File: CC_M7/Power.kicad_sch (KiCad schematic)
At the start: 18 parts, among them J13 Batt_Pins, U10 ME6211C33M5, U8 TPS562206, U9 ME6211C33M5

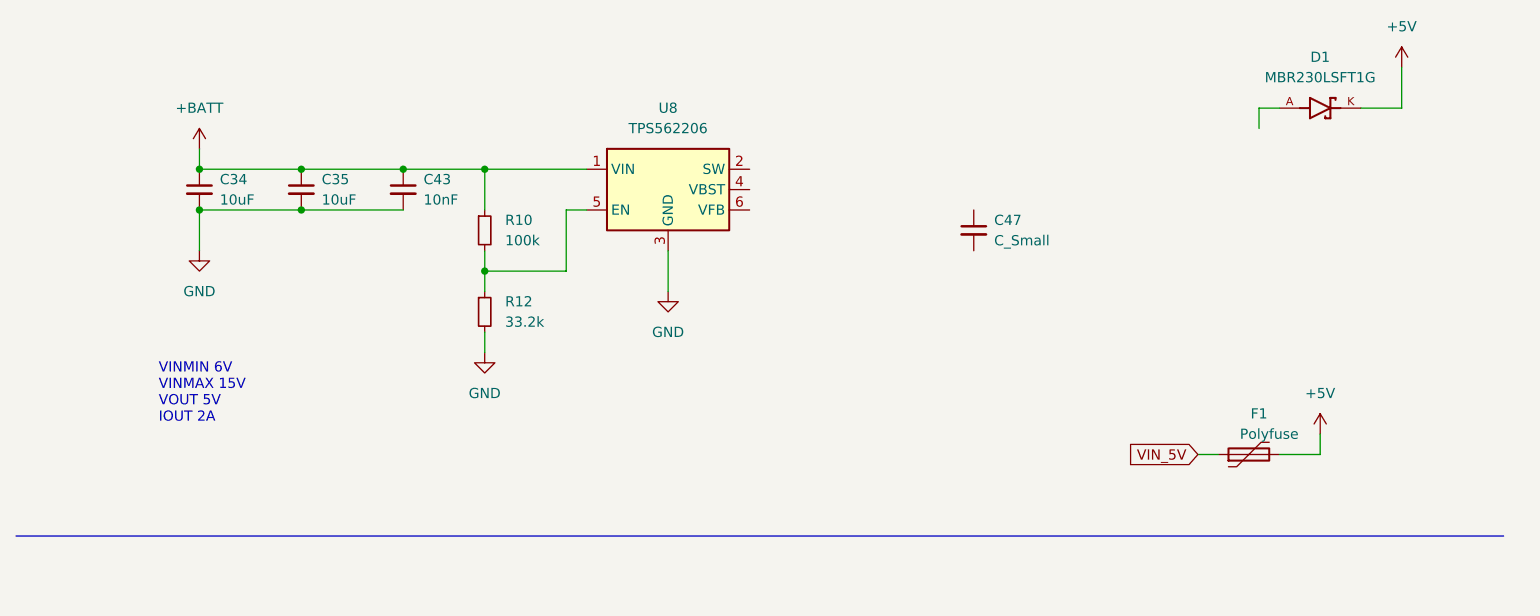
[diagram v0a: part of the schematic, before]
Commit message: New regulator tps566242DRL
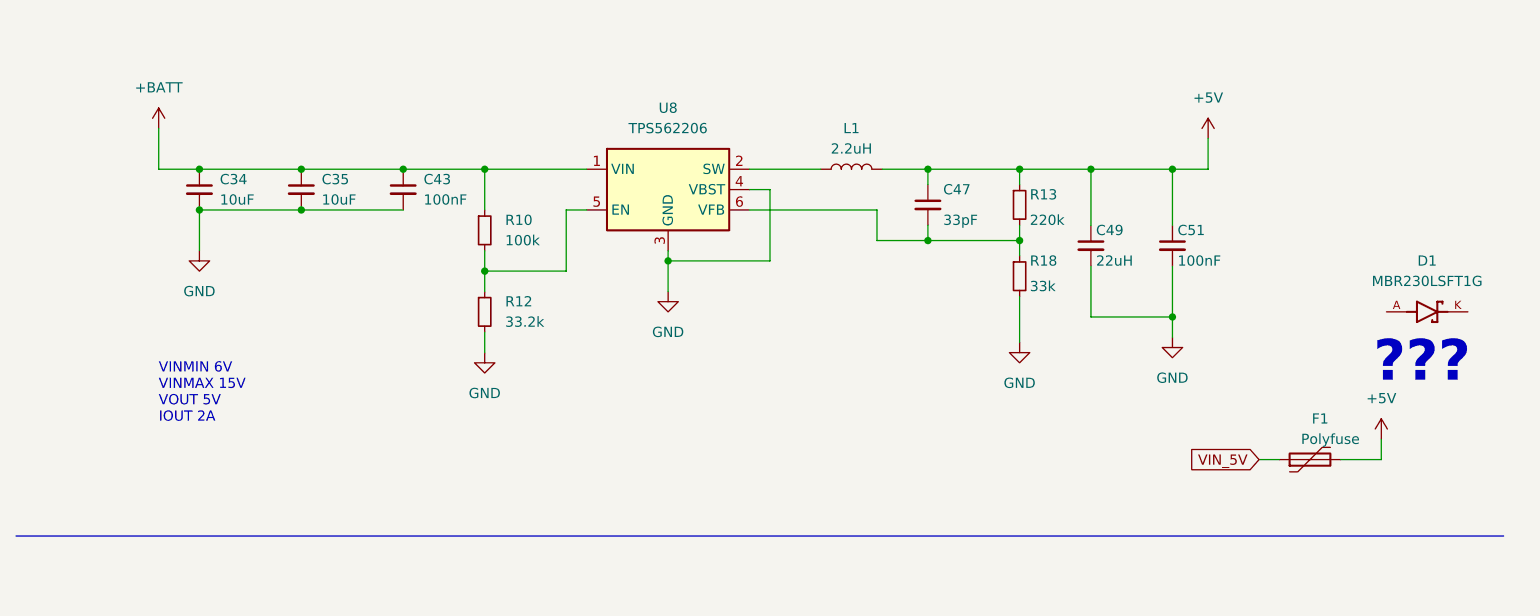
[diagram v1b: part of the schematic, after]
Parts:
- added C49: 22uH, symbol Device:C_Small
- added C51: 100nF, symbol Device:C_Small
- added L1: 2.2uH, symbol Device:L
- added R13: 220k, symbol Device:R_Small
- added R18: 33k, symbol Device:R_Small
- C43: value 10nF -> 100nF
- C47: value C_Small -> 33pF
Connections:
- net +5V: now also C47.1, C49.1, C51.1, L1.2, R13.1; no longer D1.K
- net GND: now also U8.4 (VBST), C49.2, C51.2, R18.2
- net at C47.2: now also U8.6 (VFB), R13.2, R18.1
- net at U8.2 (SW): now also L1.1
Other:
- note added: "???"
- moved on the sheet: C47, D1, F1

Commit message: Scehmatic completed.
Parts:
- added C48: 100nF, Capacitor_SMD:C_0402_1005Metric, symbol Device:C_Small
- added C53: 10uF, Capacitor_SMD:C_0603_1608Metric, symbol Device:C_Small
- added C59: 10nF, Capacitor_SMD:C_0402_1005Metric, symbol Device:C_Small
- added U12: TPS79318-EP, Package_TO_SOT_SMD:SOT-23-5, symbol Regulator_Linear:TPS79318-EP
- C34, C35, C49: footprint (none) -> Capacitor_SMD:C_0603_1608Metric
- C43, C47, C51: footprint (none) -> Capacitor_SMD:C_0402_1005Metric
- L1: footprint (none) -> Inductor_SMD:L_0402_1005Metric
- R10, R12, R13, R18: footprint (none) -> Resistor_SMD:R_0402_1005Metric
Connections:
- net +3.3V: now also C48.1, U12.1 (IN), U12.3 (EN)
- net +5V: now also D1.K; no longer C47.1, C49.1, C51.1, L1.2, R13.1
- net GND: now also C48.2, C53.2, C59.2, U12.2 (GND)
- net at D1.A: now also C47.1, C49.1, C51.1, L1.2, R13.1
- new net: C59.1, U12.4 (BP)
- new net +1V8: C53.1, U12.5 (OUT)
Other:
- note added: "12V to 5V"
- note added: "3V3 to 1V8"
- note added: "5V to 3V3"
- note removed: "???"
- moved on the sheet: D1, D2, F1, J13, R14

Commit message: ready for routing
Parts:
- removed D1: MBR230LSFT1G, MBR230LSFT1G:SODFL3619X98N, symbol MBR230LSFT1G:MBR230LSFT1G
- added D7, D8: 1N5819WS, Diode_SMD:D_SOD-323, symbol Diode:1N5819WS
- added D9: SS210, Diode_SMD:D_SOD-123, symbol Diode:SS210
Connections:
- net +3.3V: now also D7.1 (K); no longer C50.1, U10.5 (V_{OUT})
- net +5V: now also D9.1 (K)
- net 3V3_RF: now also D8.1 (K); no longer C45.1, U9.5 (V_{OUT})
- net at C47.1, C49.1, C51.1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: now also D9.2 (A)
- new net: C45.1, D8.2 (A), U9.5 (V_{OUT})
- new net: C50.1, D7.2 (A), U10.5 (V_{OUT})
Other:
- moved on the sheet: C45, C46, C47, C49, C50, C51, R13, R18, U10

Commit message: ready for routing
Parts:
- D9: footprint Diode_SMD:D_SOD-123 -> Diode_SMD:D_SOD-323
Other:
- note added: "B5819WS"
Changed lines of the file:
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@@
+		)
+	)
+	(text "B5819WS "
+		(exclude_from_sim no)
+		(at 167.64 46.99 0)
+		(effects
+			(font
+				(size 1.27 1.27)
+				(thickness 0.254)
+				(bold yes)
+			)
 		)
 	)
@@
 			)
 		)
-		(property "Footprint" "Diode_SMD:D_SOD-123"
+		(property "Footprint" "Diode_SMD:D_SOD-323"
 			(at 166.37 38.735 0)
 			(effects

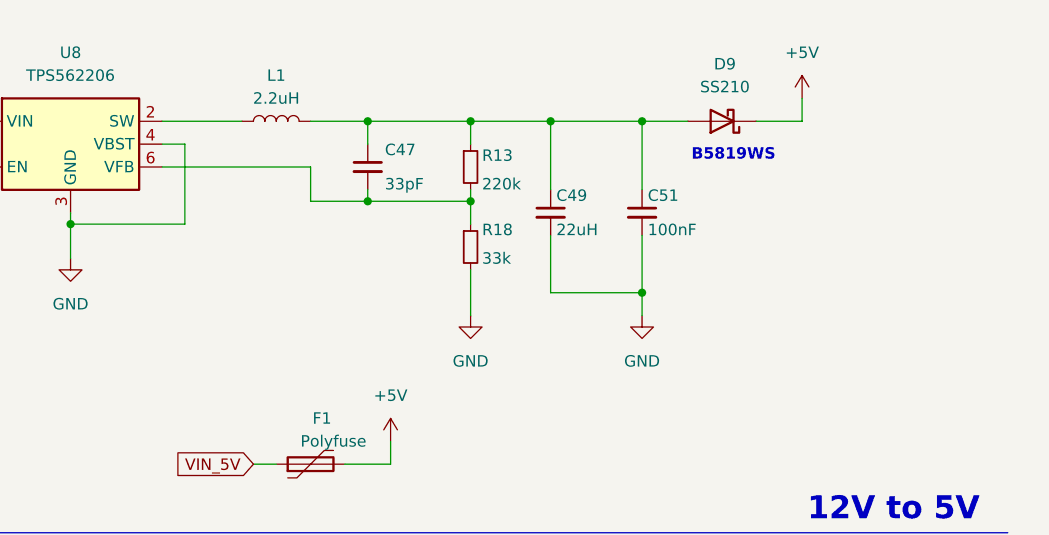
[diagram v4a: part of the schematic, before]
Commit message: Inductor added.
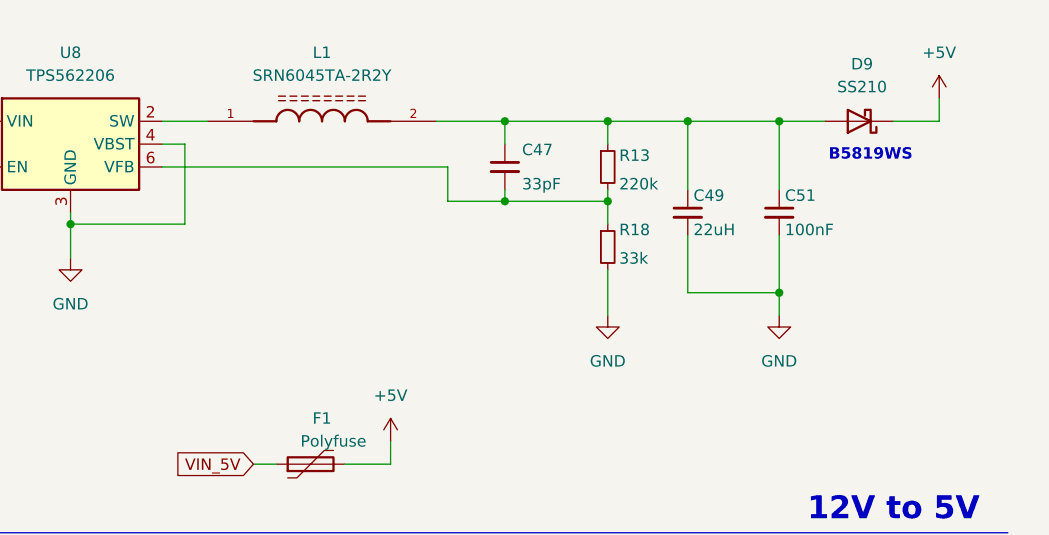
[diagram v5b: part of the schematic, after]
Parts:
- removed L1: 2.2uH, Inductor_SMD:L_0402_1005Metric, symbol Device:L
- added L1: SRN6045TA-2R2Y, 6x6mmIND:IND_SRN6045TA-2R2Y, symbol SRN6045TA-2R2Y:SRN6045TA-2R2Y
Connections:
- net at U8.2 (SW): now also L1.1
- net at C47.1, C49.1, C51.1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: now also L1.2
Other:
- moved on the sheet: C47, C49, C51, D9, R13, R18

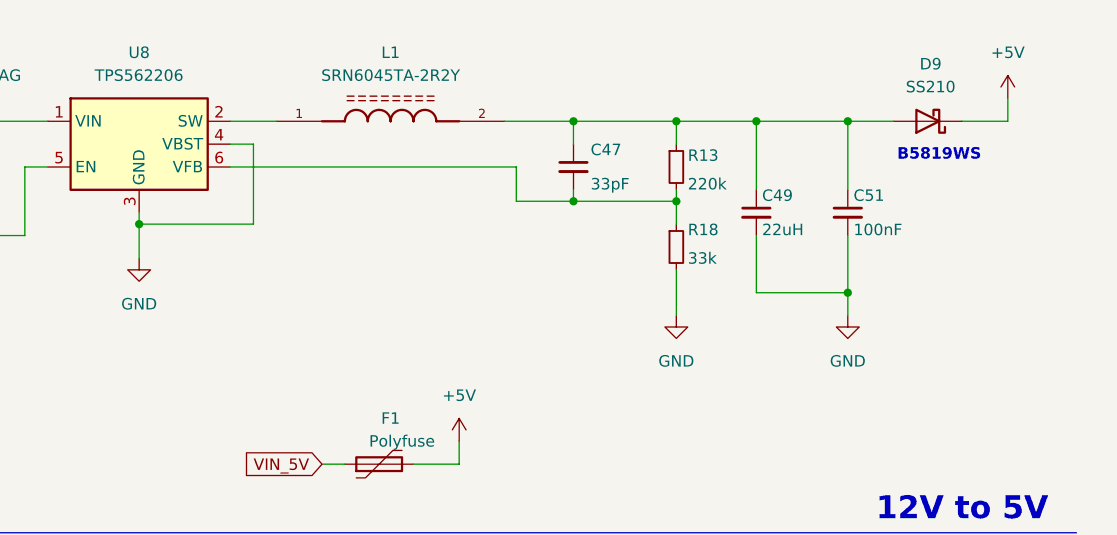
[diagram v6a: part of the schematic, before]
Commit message: regülatör devresi güvenli kullanıma uygun hale getirildi.
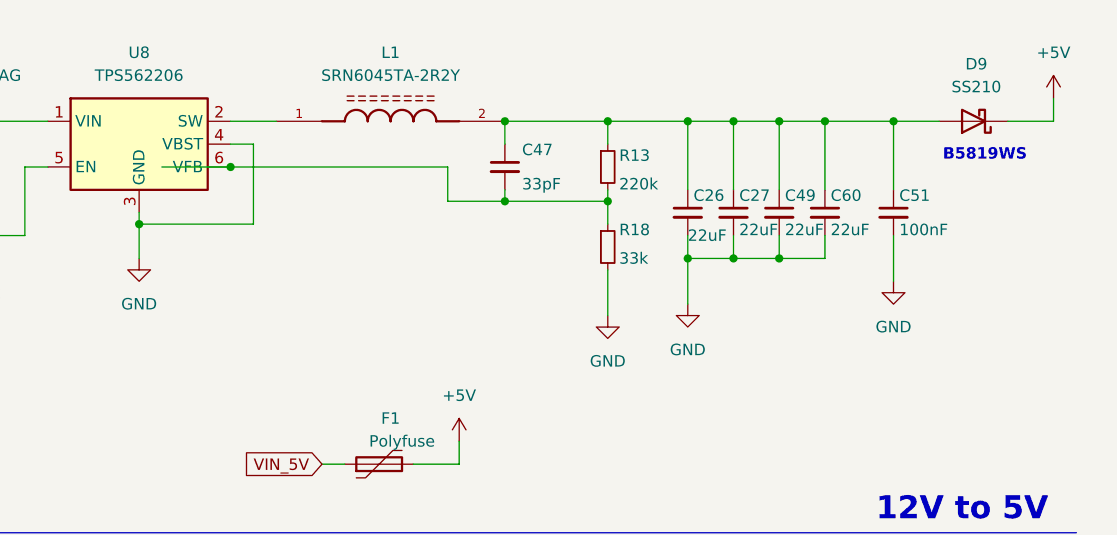
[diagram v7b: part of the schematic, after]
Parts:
- added C26, C27, C60: 22uF, Capacitor_SMD:C_0805_2012Metric, symbol Device:C_Small
- C34, C35: footprint Capacitor_SMD:C_0603_1608Metric -> Capacitor_SMD:C_0805_2012Metric
- C49: value 22uH -> 22uF; footprint Capacitor_SMD:C_0603_1608Metric -> Capacitor_SMD:C_0805_2012Metric
- C51: footprint Capacitor_SMD:C_0402_1005Metric -> Capacitor_SMD:C_0603_1608Metric
- R10, R12, R13, R18: footprint Resistor_SMD:R_0402_1005Metric -> Resistor_SMD:R_0603_1608Metric
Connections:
- net GND: now also C26.2, C27.2, C60.2
- net at C47.1, C49.1, C51.1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: now also C26.1, C27.1, C60.1
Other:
- moved on the sheet: C47, C49, C51, D9, R13, R18
